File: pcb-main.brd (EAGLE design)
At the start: 100 x 80 mm, 22 parts, among them U1 BTA-RX-A, U2 RS3-1205S

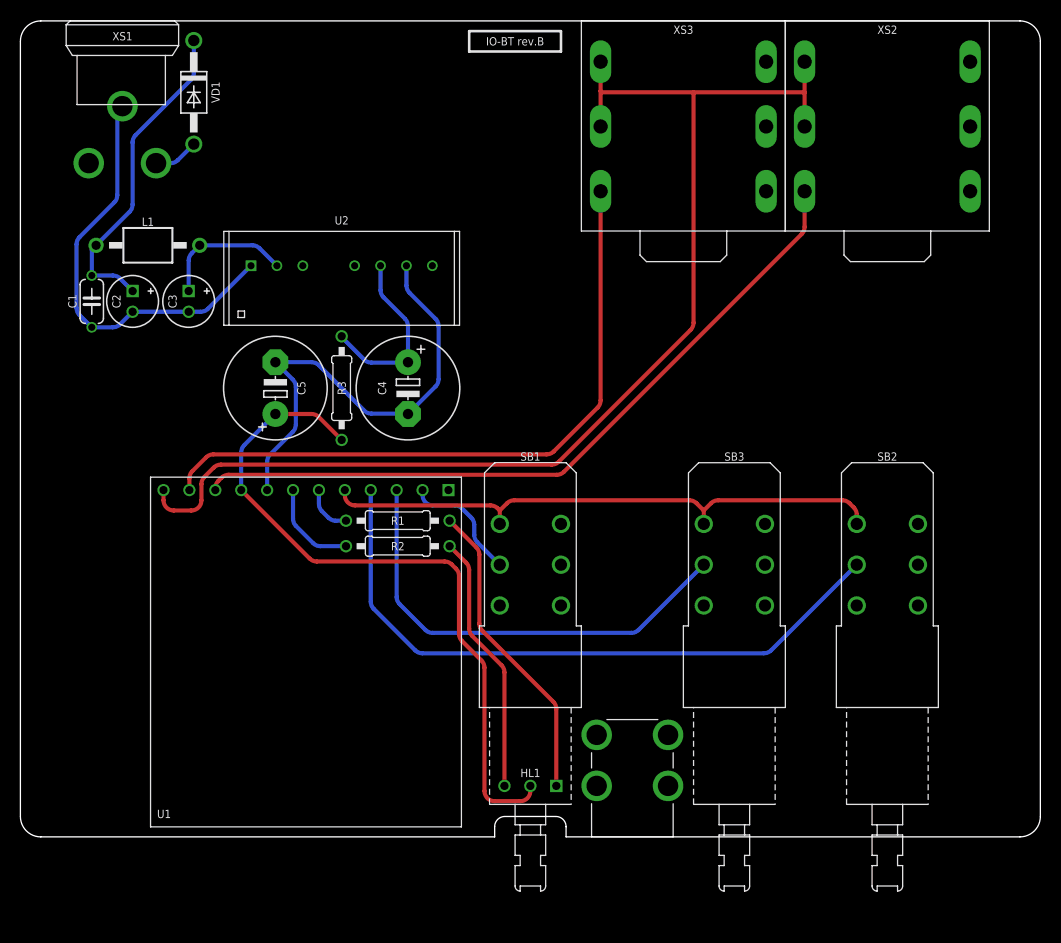
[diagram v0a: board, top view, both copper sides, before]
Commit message: Updates
- Added output volume potentiometer
- Blue LED is now used for signal indicator
- Removed next/prev buttons
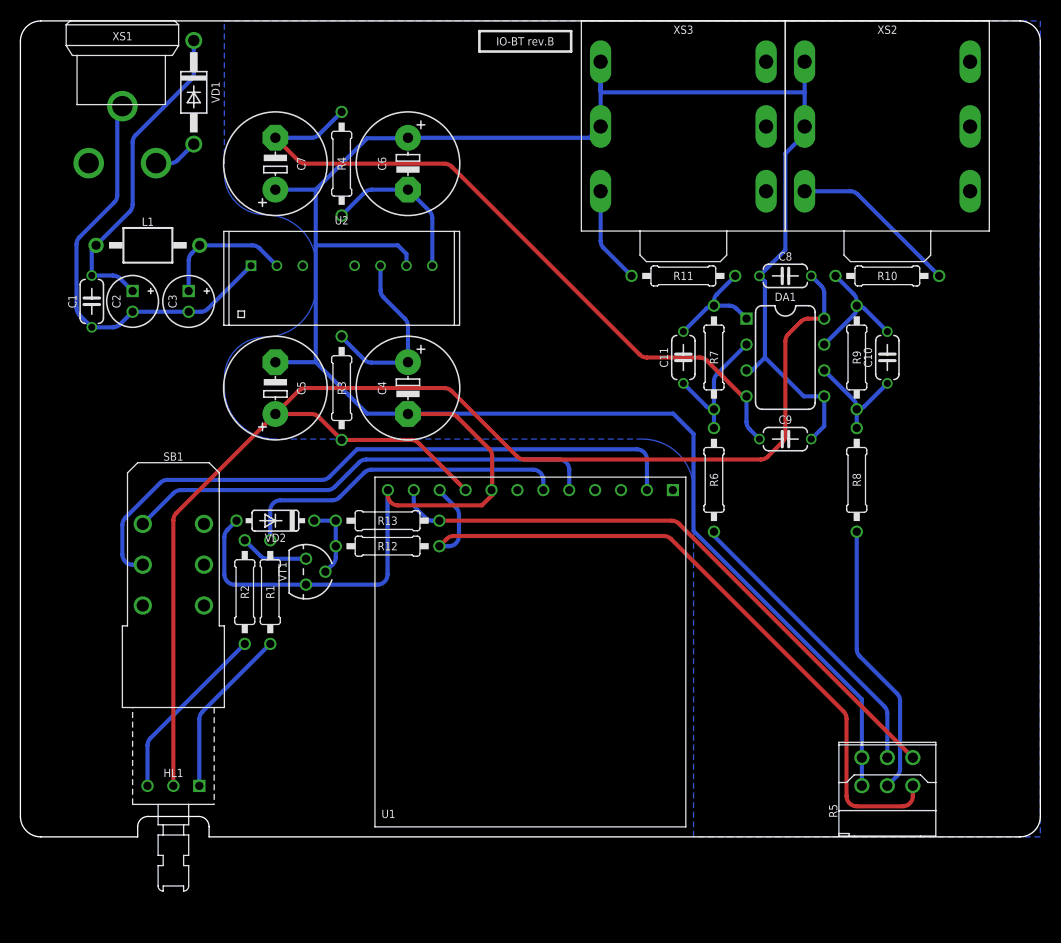
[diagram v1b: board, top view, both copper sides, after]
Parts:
- removed O1: MOUNT(KEYSTONE-7762), hardware:KEYSTONE-7762
- removed SB2, SB3: SPUN191000, switches:SPUN-DPDT
- added C10, C11: 22P(TH), capacitors:C050-024X044
- added C6, C7: 470U/35V, capacitors-electrolytic:E5-10,5
- added C8, C9: 100N(TH), capacitors:C050-024X044
- added DA1: NJM2068D, ic-jrc:DIP-8
- added R10, R11: 100R(TH), resistors:R-0207/10
- added R12, R13: 100K(TH), resistors:R-0207/10
- added R4: 2R2(TH), resistors:R-0207/10
- added R5: 2*A10K(PTD90), potentiometers:PTD902
- added R6, R7, R8, R9: 10K(TH), resistors:R-0207/10
- added VD2: 1N4148, diodes:DO35-7
- added VT1: BC548, transistors-npn:TO92
- R1, R2: value 1K(TH) -> 1K5(TH)
- U2: value RS3-1205S -> RS3-1205D
- moved HL1 35.0 mm to (15.0, 5.00)
- moved SB1 35.0 mm to (15.0, 3.00)
- moved U1 22.0 mm to (50.0, 34.0)
- moved R2 15.7 mm to (22.0, 24.0), turned to 90 degrees
- moved R1 14.3 mm to (24.5, 24.0), turned to 90 degrees
- moved PCB1 1.00 mm to (49.5, 78.0)
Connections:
- removed net N$35: U1.12, XS2.R, XS2.S, XS3.R, XS3.S
- removed net N$36: U1.10, XS2.T
- removed net N$37: U1.11, XS3.T
- removed net N$45: R2.2, U1.7
- new net -5V: C7.-, C9.1, DA1.4, R4.2
- new net N$10: R10.2, XS2.T
- new net N$11: R11.2, XS3.T
- new net N$12: R2.2, VT1.1
- new net N$13: R12.2, R13.2, VD2.C, VT1.2
- new net N$3: R5.B2, R6.1
- new net N$4: C11.1, DA1.2, R6.2, R7.1
- new net N$5: C10.1, DA1.6, R8.2, R9.1
- new net N$6: R12.1, R5.A3, U1.10
- new net N$7: R13.1, R5.B3, U1.11
- new net N$8: C10.2, DA1.7, R10.1, R9.2
- new net N$9: C11.2, DA1.1, R11.1, R7.2
- net +5V: now also C8.2, DA1.8
- net GND: now also C6.+, C7.+, C8.1, C9.2, DA1.3, DA1.5, R5.A1, R5.B1, U1.12, VD2.A, VT1.3, XS2.R, XS2.S, XS3.R, XS3.S
- net N$1: now also C6.-, R4.1, U2.8; no longer SB2.2, U1.4
- net N$2: now also R5.A2, R8.1; no longer SB3.2, U1.3
- net N$41: no longer SB2.3, SB3.3
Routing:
- net GND: track 46.2 -> 278.3 mm
- net N$35: track 117.5 -> 0.00 mm
- net N$36: track 72.3 -> 0.00 mm
- net N$6: track 0.00 -> 71.3 mm
- net -5V: track 0.00 -> 68.6 mm
- net +5V: track 69.0 -> 135.7 mm
- net N$37: track 65.4 -> 0.00 mm
- net N$7: track 0.00 -> 60.5 mm
- net N$38: track 11.8 -> 63.3 mm
- net N$1: track 64.3 -> 15.9 mm
- net N$3: track 0.00 -> 29.1 mm
- net N$44: track 4.80 -> 32.6 mm
- net N$2: track 44.9 -> 27.0 mm
- net N$10: track 0.00 -> 16.6 mm
- net N$4: track 0.00 -> 13.4 mm
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- added copper zone on layer 16, net GND
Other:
- outline, holes or cut-outs redrawn

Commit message: Change switch position
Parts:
- moved SB1 3.00 mm to (15.0, 0.00)
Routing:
- net N$41: track 46.7 -> 49.3 mm
- net N$38: track 63.3 -> 65.6 mm
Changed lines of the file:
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@@
 <layer number="45" name="Holes" color="7" fill="1" visible="no" active="yes"/>
 <layer number="46" name="Milling" color="3" fill="1" visible="no" active="yes"/>
-<layer number="47" name="Measures" color="7" fill="1" visible="no" active="yes"/>
+<layer number="47" name="Measures" color="7" fill="1" visible="yes" active="yes"/>
 <layer number="48" name="Document" color="7" fill="1" visible="yes" active="yes"/>
 <layer number="49" name="Reference" color="7" fill="1" visible="yes" active="yes"/>
@@
 </element>
 <element name="U1" library="module-wireless" package="BTA-RX" value="BTA-RX-A" x="50" y="34" rot="R180"/>
-<element name="SB1" library="switches" package="SPUN-DPDT" value="SPUN191000" x="15" y="3" rot="R180"/>
+<element name="SB1" library="switches" package="SPUN-DPDT" value="SPUN191000" x="15" y="0" rot="R180"/>
 <element name="HL1" library="optoelectronics" package="DUOLED3MM-H" value="RED/BLUE(3MM,CA)" x="15" y="5" rot="R180"/>
 <element name="R1" library="resistors" package="R-0207/10" value="1K5(TH)" x="24.5" y="24" rot="R90">
@@
 <contactref element="SB1" pad="2"/>
 <contactref element="U1" pad="2"/>
-<wire x1="12" y1="26.685" x2="11" y2="26.685" width="0.4064" layer="16"/>
-<wire x1="11" y1="26.685" x2="10" y2="27.685" width="0.4064" layer="16" curve="-90"/>
-<wire x1="10" y1="27.685" x2="10" y2="30.5857875" width="0.4064" layer="16"/>
+<wire x1="12" y1="23.685" x2="10.29289375" y2="25.39210625" width="0.4064" layer="16"/>
+<wire x1="10.29289375" y1="25.39210625" x2="10" y2="26.0992125" width="0.4064" layer="16" curve="-45"/>
+<wire x1="10" y1="26.0992125" x2="10" y2="30.5857875" width="0.4064" layer="16"/>
 <wire x1="10" y1="30.5857875" x2="10.29289375" y2="31.29289375" width="0.4064" layer="16" curve="-45"/>
 <wire x1="10.29289375" y1="31.29289375" x2="13.70710625" y2="34.70710625" width="0.4064" layer="16"/>
@@
 <wire x1="33.20710625" y1="36.70710625" x2="30.79289375" y2="34.29289375" width="0.4064" layer="16"/>
 <wire x1="30.79289375" y1="34.29289375" x2="30.0857875" y2="34" width="0.4064" layer="16" curve="-45"/>
-<wire x1="30.0857875" y1="34" x2="15.7292125" y2="34" width="0.4064" layer="16"/>
-<wire x1="15.7292125" y1="34" x2="15.02210625" y2="33.70710625" width="0.4064" layer="16" curve="45"/>
-<wire x1="15.02210625" y1="33.70710625" x2="12" y2="30.685" width="0.4064" layer="16"/>
+<wire x1="30.0857875" y1="34" x2="16.143425" y2="34" width="0.4064" layer="16"/>
+<wire x1="16.143425" y1="34" x2="15.43631875" y2="33.70710625" width="0.4064" layer="16" curve="45"/>
+<wire x1="15.43631875" y1="33.70710625" x2="12.29289375" y2="30.56368125" width="0.4064" layer="16"/>
+<wire x1="12.29289375" y1="30.56368125" x2="12" y2="29.856575" width="0.4064" layer="16" curve="45"/>
+<wire x1="12" y1="29.856575" x2="12" y2="27.685" width="0.4064" layer="16"/>
 </signal>
 <signal name="N$42">
